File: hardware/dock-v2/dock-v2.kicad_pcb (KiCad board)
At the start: 4 copper layers, 148 parts, among them J101 TYPE-C-31-M-12, J201 TYPE-C-31-M-12, J202 TYPE-C-31-M-12, J203 TYPE-C-31-M-12, J601 Pogo 7-pin, Q601 2N7002, Q602 2N7002, SW301 SW_Push, SW302 SW_Push, SW401 SW_Push, U101 TPD4E1U06DBVR, U102 CH224A, U103 TPS54331DR, U104 AMS1117-3.3, U201 TPD4E1U06DBVR, U202 SY6280AAC, U203 TPD4E1U06DBVR, U204 TPD4E1U06DBVR, U301 RP2354A, U401 RP2354A, U501 ESP32-C3-MINI-1-H4X, U601 TPD4E1U06DBVR, U602 SY6280AAC, Y301 12MHz, Y401 12MHz

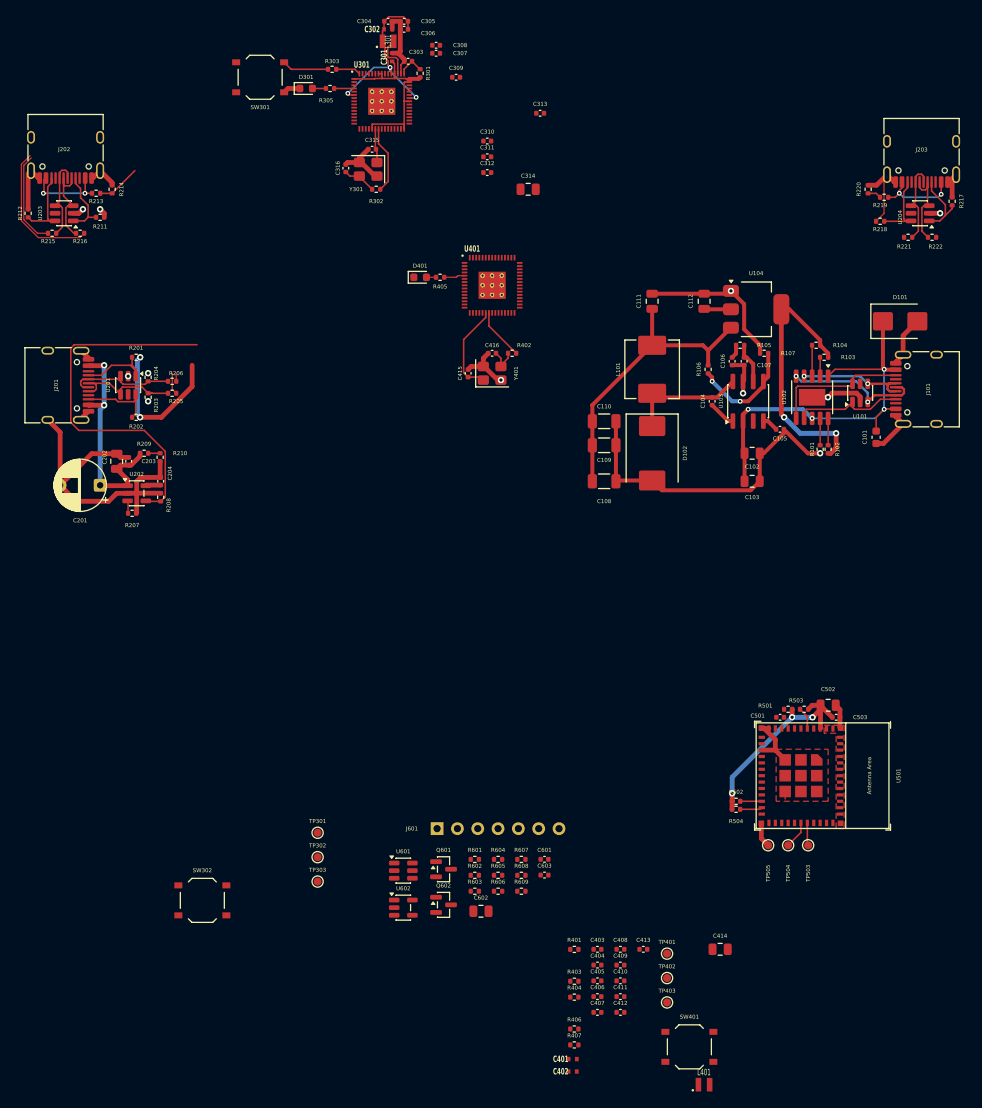
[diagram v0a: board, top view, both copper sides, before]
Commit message: Dock v2 PCB: 100 x 100 mm working outline (129,35)-(229,135), centred on the parts
Co-Authored-By: Claude Opus 5.5 <noreply@anthropic.com>
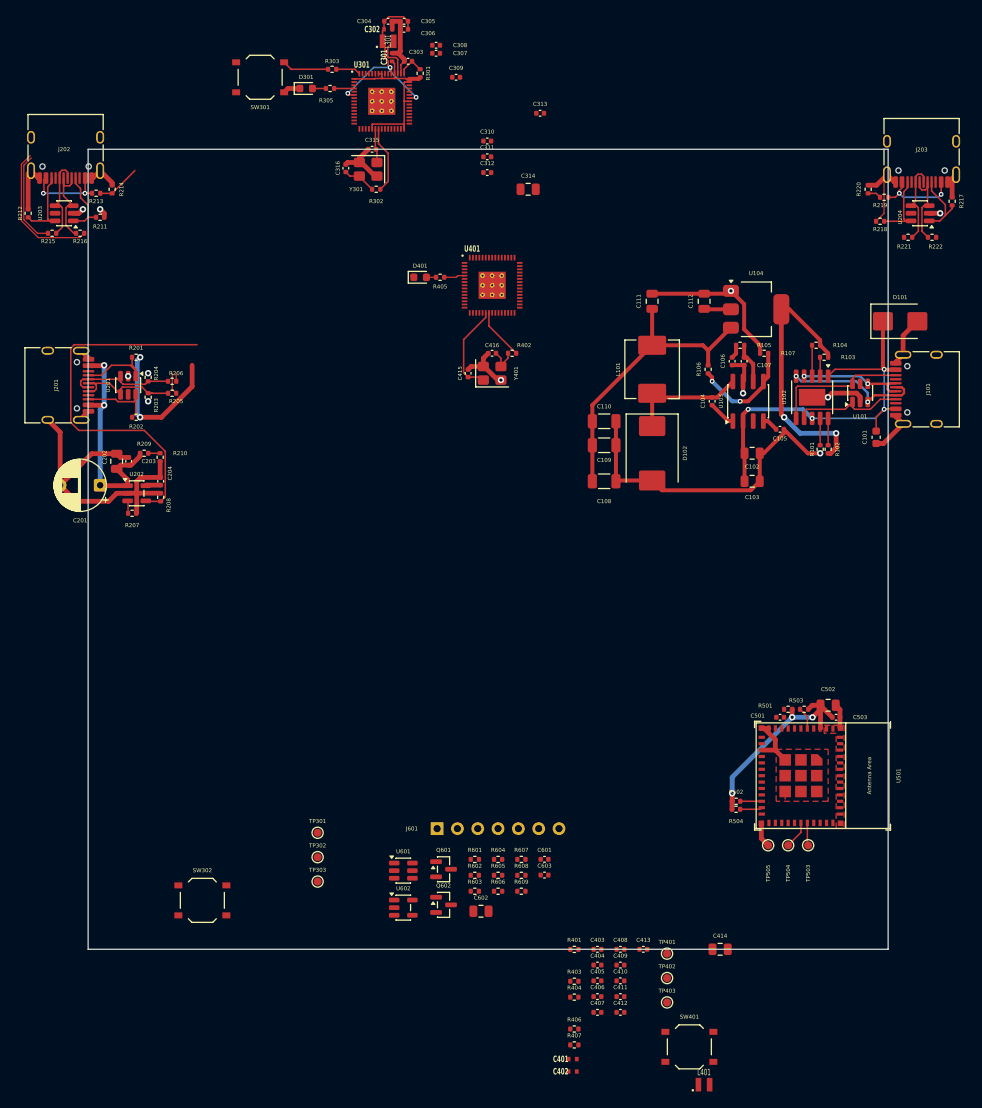
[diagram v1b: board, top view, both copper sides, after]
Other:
- board outline added: 100 x 100 mm
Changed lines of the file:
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@@
 		)
+	)
+	(gr_rect
+		(start 129 35)
+		(end 229 135)
+		(stroke
+			(width 0.05)
+			(type default)
+		)
+		(fill no)
+		(layer "Edge.Cuts")
 	)
 	(footprint "Capacitor_SMD:C_0805_2012Metric"
